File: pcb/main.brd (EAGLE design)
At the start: 58 x 52 mm, 81 parts, among them IC1 NC7SZ14M5X, IC2 LSM303DLHC, J3 455-1750-1-ND, J6 M1 connector, J7 M2 connector, Q1 2.5A/30V/105mΩ, U5 ESP-WROOM-32

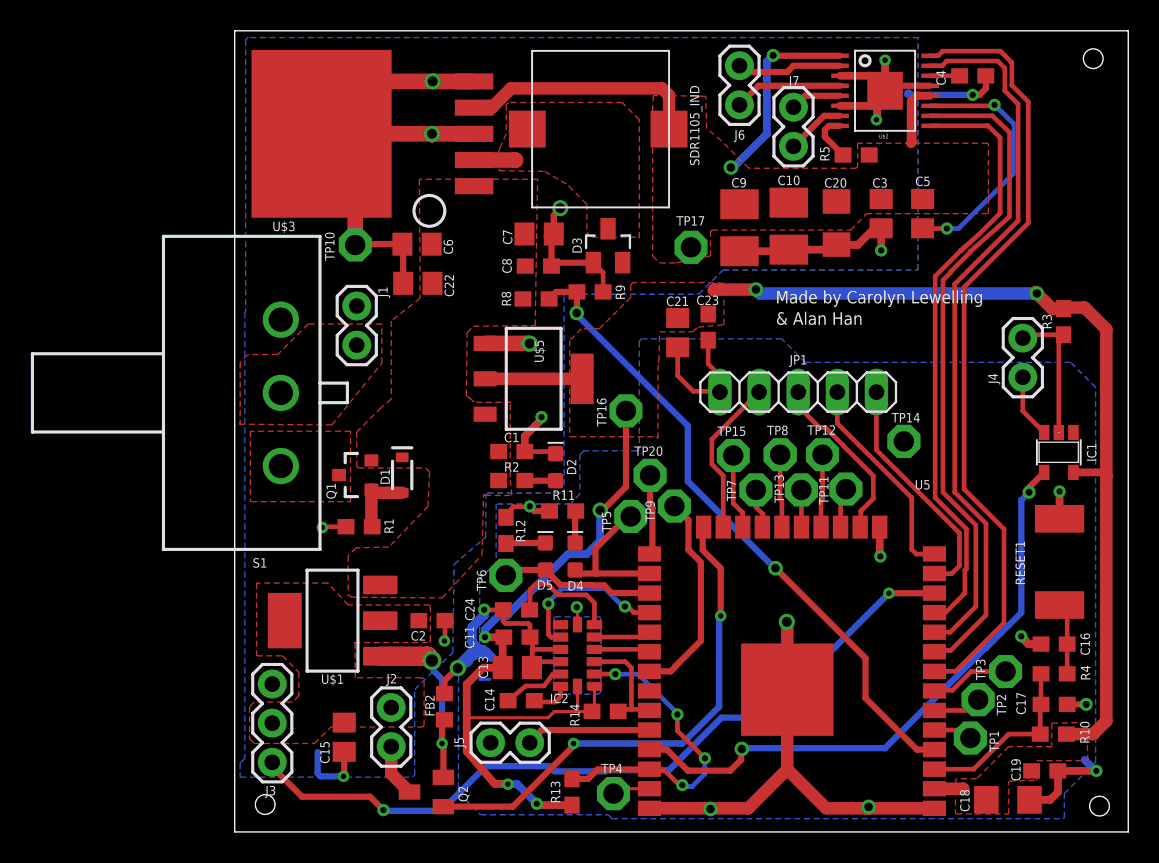
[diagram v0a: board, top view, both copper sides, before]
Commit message: fixes for rev2
fixed mounting holes, connector overlap, added 6th pin for jtag,
isolated 3rd switch pin, and added push button for IO0
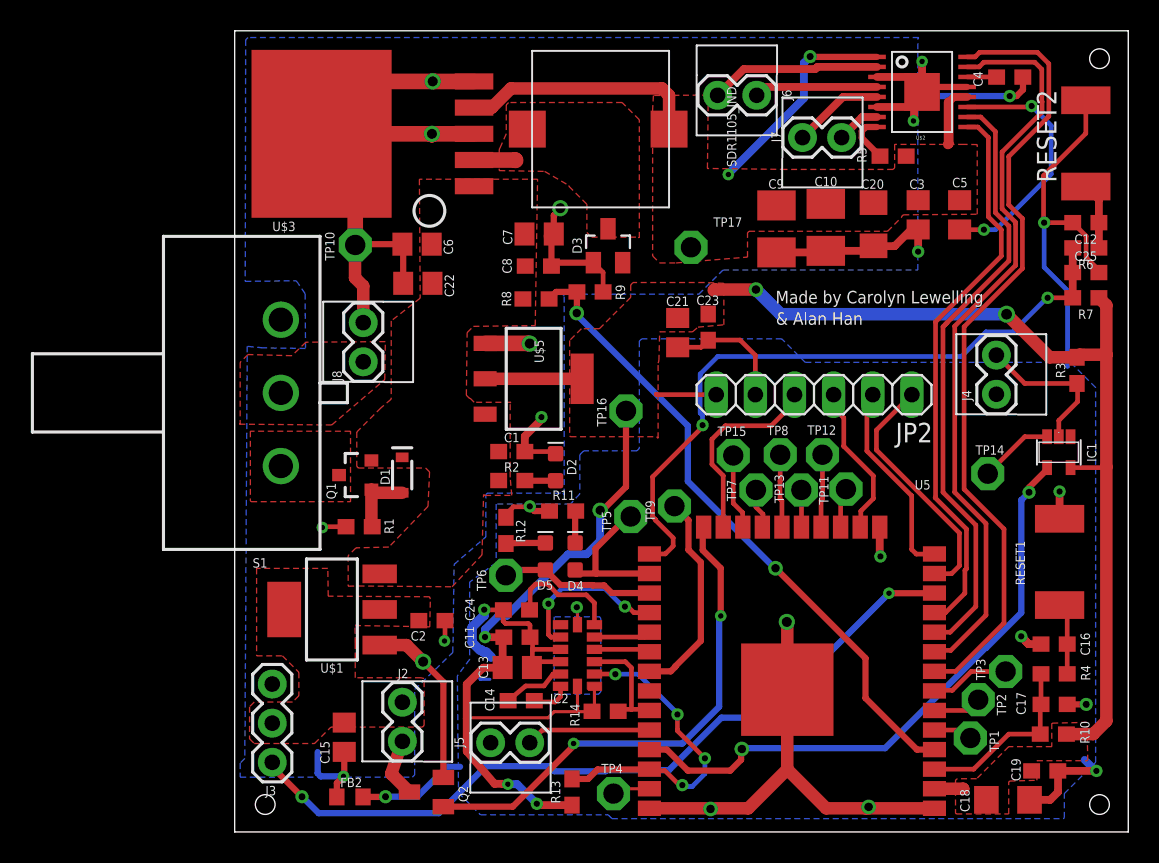
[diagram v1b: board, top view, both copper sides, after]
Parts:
- removed J1: (no value), electricSheepParty:1X02
- removed JP1: (no value), pinhead:1X05
- removed TP20: TPPAD1-13, testpad:P1-13
- added C12, C25: 1nF, electricSheepParty:0603
- added J8: (no value), electricSheepParty:1X02
- added JP2: (no value), pinhead:1X06
- added R6, R7: 470, electricSheepParty:0603
- added RESET2: S2, DiscreteComponents:SW_2512
- moved FB2 8.48 mm to (7.48, 2.27), turned to 0 degrees
- moved TP14 5.84 mm to (48.9, 23.3)
- moved R3 3.28 mm to (54.7, 30.0)
- moved C10 2.40 mm to (38.4, 39.2)
- moved C20 2.40 mm to (41.5, 39.4)
- moved C3 2.40 mm to (44.4, 40.1)
- moved C5 2.40 mm to (47.1, 40.1)
- moved C9 2.40 mm to (35.2, 39.1)
- moved R5 2.40 mm to (42.7, 43.9)
- moved U$2 2.40 mm to (44.6, 48.0)
- moved C4 2.40 mm to (50.3, 49.0)
- moved J7 2.05 mm to (36.9, 45.1), turned to 0 degrees
- moved J4 2.04 mm to (49.4, 28.4)
- moved J6 1.28 mm to (33.9, 47.8), turned to 180 degrees
- moved J2 0.80 mm to (10.9, 5.88)
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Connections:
- removed net N$27: TP20.TP, U5.25
- new net IO0: C25.1, R6.2, R7.2, U5.25
- new net N$6: C12.1, R6.1, RESET2.1
- net 3V3: now also JP2.6, R7.1
- net 6V_RAW: now also J8.1; no longer J1.2
- net AGND: now also J8.2; no longer J1.1
- net GND: now also C12.2, C25.2, JP2.5, RESET2.2; no longer JP1.5
- net TCK: now also JP2.3; no longer JP1.3
- net TDI: now also JP2.2; no longer JP1.2
- net TDO: now also JP2.4; no longer JP1.4
- net TMS: now also JP2.1; no longer JP1.1
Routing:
- net IO0: track 0.00 -> 44.6 mm, vias 0 -> 2
- net GND: track 80.6 -> 108.7 mm, vias 12 -> 13
- net AGND: track 91.7 -> 99.4 mm, vias 14 -> 13
- net 3V3: track 116.2 -> 123.1 mm
- net N$27: track 5.24 -> 0.00 mm
- net N$6: track 0.00 -> 4.33 mm
- net M1+: track 6.86 -> 11.1 mm
- net PWM_M2A: track 39.6 -> 36.7 mm
- net PWM_M2B: track 42.5 -> 39.6 mm
- net M2-: track 3.33 -> 5.93 mm
- net TDO: track 10.3 -> 12.9 mm
- net TCK: track 11.4 -> 10.0 mm
- net 3V3M: track 32.5 -> 33.8 mm
- net M1-: track 7.04 -> 8.03 mm
- net M2+: track 3.84 -> 2.85 mm
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
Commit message: moved sheepy
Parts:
- moved C20 4.43 mm to (37.0, 39.1)
- moved C10 4.01 mm to (34.4, 39.0)
- moved C9 3.85 mm to (31.3, 39.0)
- moved TP17 1.62 mm to (28.0, 38.2)
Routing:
- net AGND: track 99.4 -> 102.6 mm
